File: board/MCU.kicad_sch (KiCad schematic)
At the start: 19 parts, among them J1 DEBUG, Q1 NMOS, Q2 BSS138, U4 LT1910, U7 ESP32-S2-DEVKITM-1U

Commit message: Add TFT Molex Connector
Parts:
- C3: footprint (none) -> Capacitor_SMD:C_0603_1608Metric_Pad1.08x0.95mm_HandSolder
- R16, R17, R3: footprint (none) -> Resistor_SMD:R_0603_1608Metric_Pad0.98x0.95mm_HandSolder
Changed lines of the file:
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@@
 			)
 		)
-		(property "Footprint" ""
+		(property "Footprint" "Capacitor_SMD:C_0603_1608Metric_Pad1.08x0.95mm_HandSolder"
 			(at 144.78 166.37 0)
 			(effects
@@
 			)
 		)
-		(property "Footprint" ""
+		(property "Footprint" "Resistor_SMD:R_0603_1608Metric_Pad0.98x0.95mm_HandSolder"
 			(at 241.046 34.544 90)
 			(effects
@@
 			)
 		)
-		(property "Footprint" ""
+		(property "Footprint" "Resistor_SMD:R_0603_1608Metric_Pad0.98x0.95mm_HandSolder"
 			(at 246.634 34.036 90)
 			(effects
@@
 			)
 		)
-		(property "Footprint" ""
+		(property "Footprint" "Resistor_SMD:R_0603_1608Metric_Pad0.98x0.95mm_HandSolder"
 			(at 108.966 143.764 90)
 			(effects

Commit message: Add Footprint Assignments
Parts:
- B1: footprint (none) -> MRDT_Devices:BUZZER_SMI_1324_TW_5V_2_R
- C5: footprint Capacitor_SMD:C_0603_1608Metric_Pad1.08x0.95mm_HandSolder -> Capacitor_THT:CP_Radial_D10.0mm_P5.00mm
- Conn5: footprint MRDT_Connectors:MOLEX_SL_04_Vertical -> MRDT_Connectors:MOLEX_SL_09_Horizontal
- Conn6: footprint (none) -> MRDT_Connectors:MOLEX_SL_07_Horizontal
- J1: footprint (none) -> Connector_PinSocket_2.54mm:PinSocket_1x04_P2.54mm_Vertical
- Molex4_1, Molex4_4, Molex4_6, Molex4_7: footprint MRDT_Connectors:MOLEX_SL_04_Vertical -> MRDT_Connectors:MOLEX_SL_04_Horizontal
- Q1: footprint (none) -> Package_TO_SOT_THT:TO-220-3_Vertical
- U4: footprint (none) -> Package_SO:SOIC-8_3.9x4.9mm_P1.27mm
- U7: footprint ESP32-S2-DEVKITM-1U:XCVR_ESP32-S2-DEVKITM-1U -> MRDT_Shields:XCVR_ESP32-S2-DEVKITM-1U
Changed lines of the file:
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@@
 			)
 		)
-		(property "Footprint" ""
+		(property "Footprint" "MRDT_Devices:BUZZER_SMI_1324_TW_5V_2_R"
 			(at 46.99 167.64 0)
 			(effects
@@
 			)
 		)
-		(property "Footprint" ""
+		(property "Footprint" "MRDT_Connectors:MOLEX_SL_07_Horizontal"
 			(at 218.44 119.38 0)
 			(effects
@@
 			)
 		)
-		(property "Footprint" "MRDT_Connectors:MOLEX_SL_04_Vertical"
+		(property "Footprint" "MRDT_Connectors:MOLEX_SL_04_Horizontal"
 			(at 257.81 46.99 0)
 			(effects
@@
 			)
 		)
-		(property "Footprint" "Capacitor_SMD:C_0603_1608Metric_Pad1.08x0.95mm_HandSolder"
+		(property "Footprint" "Capacitor_THT:CP_Radial_D10.0mm_P5.00mm"
 			(at 44.1452 93.98 0)
 			(effects
@@
 			)
 		)
-		(property "Footprint" "MRDT_Connectors:MOLEX_SL_04_Vertical"
+		(property "Footprint" "MRDT_Connectors:MOLEX_SL_04_Horizontal"
 			(at 266.7 74.93 0)
 			(effects
@@
 			)
 		)
-		(property "Footprint" "MRDT_Connectors:MOLEX_SL_04_Vertical"
+		(property "Footprint" "MRDT_Connectors:MOLEX_SL_04_Horizontal"
 			(at 264.16 138.43 0)
 			(effects
@@
 			)
 		)
-		(property "Footprint" ""
+		(property "Footprint" "Package_TO_SOT_THT:TO-220-3_Vertical"
 			(at 165.1 157.48 0)
 			(effects
@@
 			)
 		)
-		(property "Footprint" "MRDT_Connectors:MOLEX_SL_04_Vertical"
+		(property "Footprint" "MRDT_Connectors:MOLEX_SL_09_Horizontal"
 			(at 22.86 50.8 0)
 			(effects
@@
 			)
 		)
-		(property "Footprint" "MRDT_Connectors:MOLEX_SL_04_Vertical"
+		(property "Footprint" "MRDT_Connectors:MOLEX_SL_04_Horizontal"
 			(at 266.7 109.22 0)
 			(effects
@@
 			)
 		)
-		(property "Footprint" ""
+		(property "Footprint" "Package_SO:SOIC-8_3.9x4.9mm_P1.27mm"
 			(at 118.11 162.56 0)
 			(effects
@@
 			)
 		)
-		(property "Footprint" ""
+		(property "Footprint" "Connector_PinSocket_2.54mm:PinSocket_1x04_P2.54mm_Vertical"
 			(at 213.36 34.29 0)
 			(effects
@@
 			)
 		)
-		(property "Footprint" "ESP32-S2-DEVKITM-1U:XCVR_ESP32-S2-DEVKITM-1U"
+		(property "Footprint" "MRDT_Shields:XCVR_ESP32-S2-DEVKITM-1U"
 			(at 127 64.77 0)
 			(effects

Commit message: Add Layout
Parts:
- Conn2, Conn3: footprint MRDT_Connectors:Anderson_2_Horizontal_Side_by_Side -> MRDT_Connectors:Square_Anderson_2_H_Side_By_Side_PV
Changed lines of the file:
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@@
 			)
 		)
-		(property "Footprint" "MRDT_Connectors:Anderson_2_Horizontal_Side_by_Side"
+		(property "Footprint" "MRDT_Connectors:Square_Anderson_2_H_Side_By_Side_PV"
 			(at 30.48 139.7 0)
 			(effects
@@
 			)
 		)
-		(property "Footprint" "MRDT_Connectors:Anderson_2_Horizontal_Side_by_Side"
+		(property "Footprint" "MRDT_Connectors:Square_Anderson_2_H_Side_By_Side_PV"
 			(at 22.86 113.03 0)
 			(effects
@@
 			)
 		)
-		(property "Footprint" "MRDT_Connectors:Anderson_2_Horizontal_Side_by_Side"
+		(property "Footprint" "MRDT_Connectors:Square_Anderson_2_H_Side_By_Side_PV"
 			(at 22.86 101.6 0)
 			(effects
@@
 			)
 		)
-		(property "Footprint" "MRDT_Connectors:Anderson_2_Horizontal_Side_by_Side"
+		(property "Footprint" "MRDT_Connectors:Square_Anderson_2_H_Side_By_Side_PV"
 			(at 30.48 148.59 0)
 			(effects

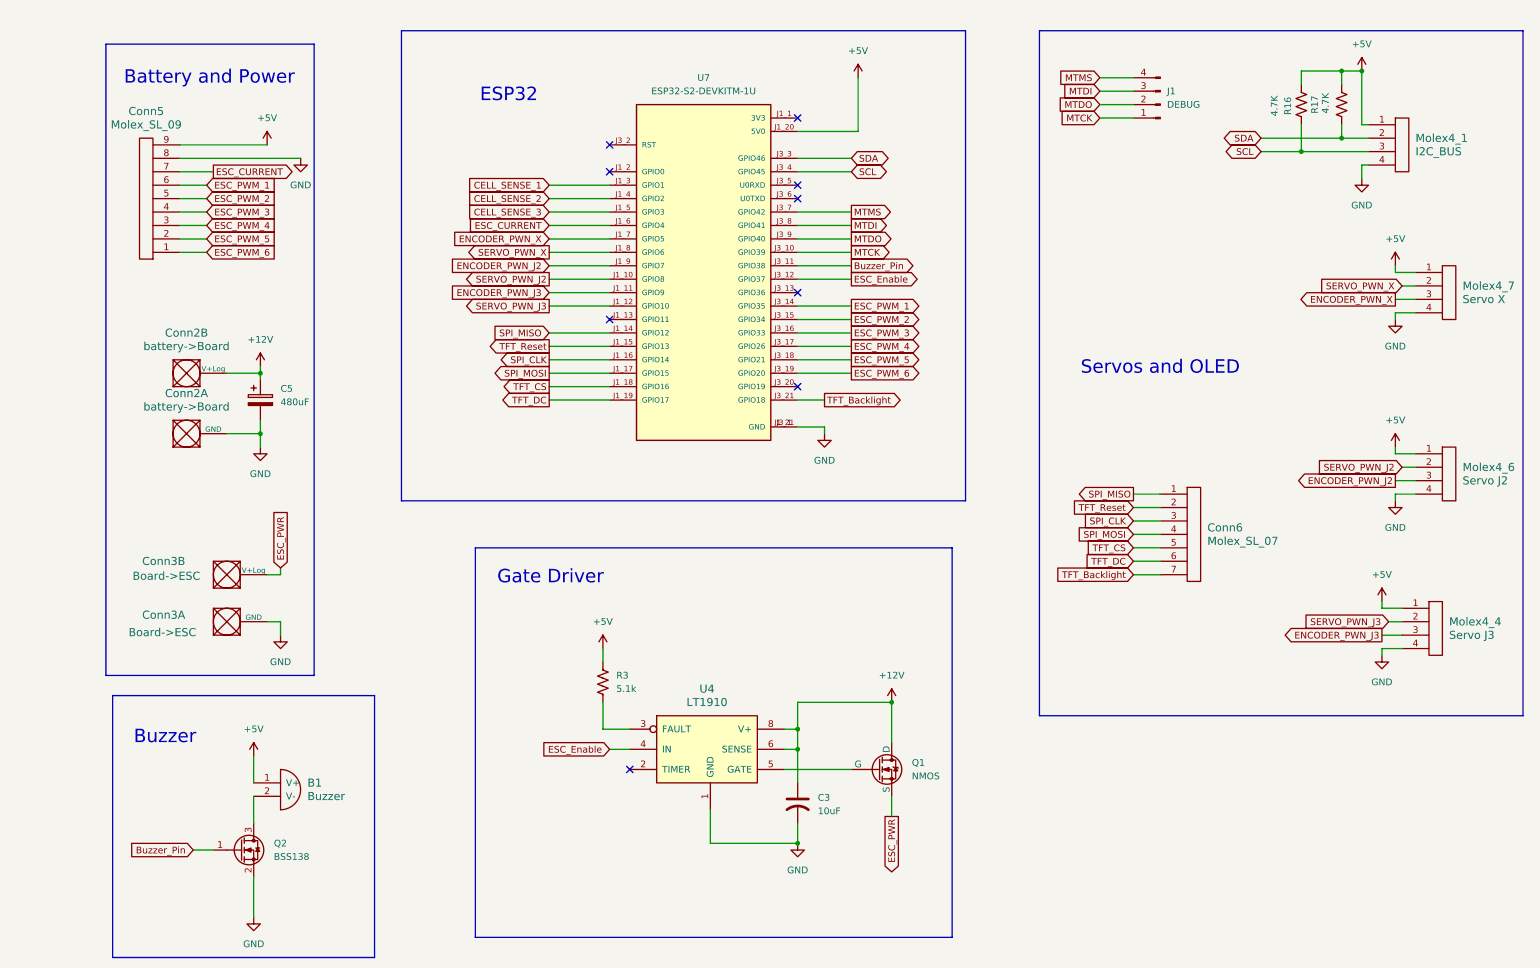
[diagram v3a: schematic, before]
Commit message: added pmos channel (still need footprints not working)
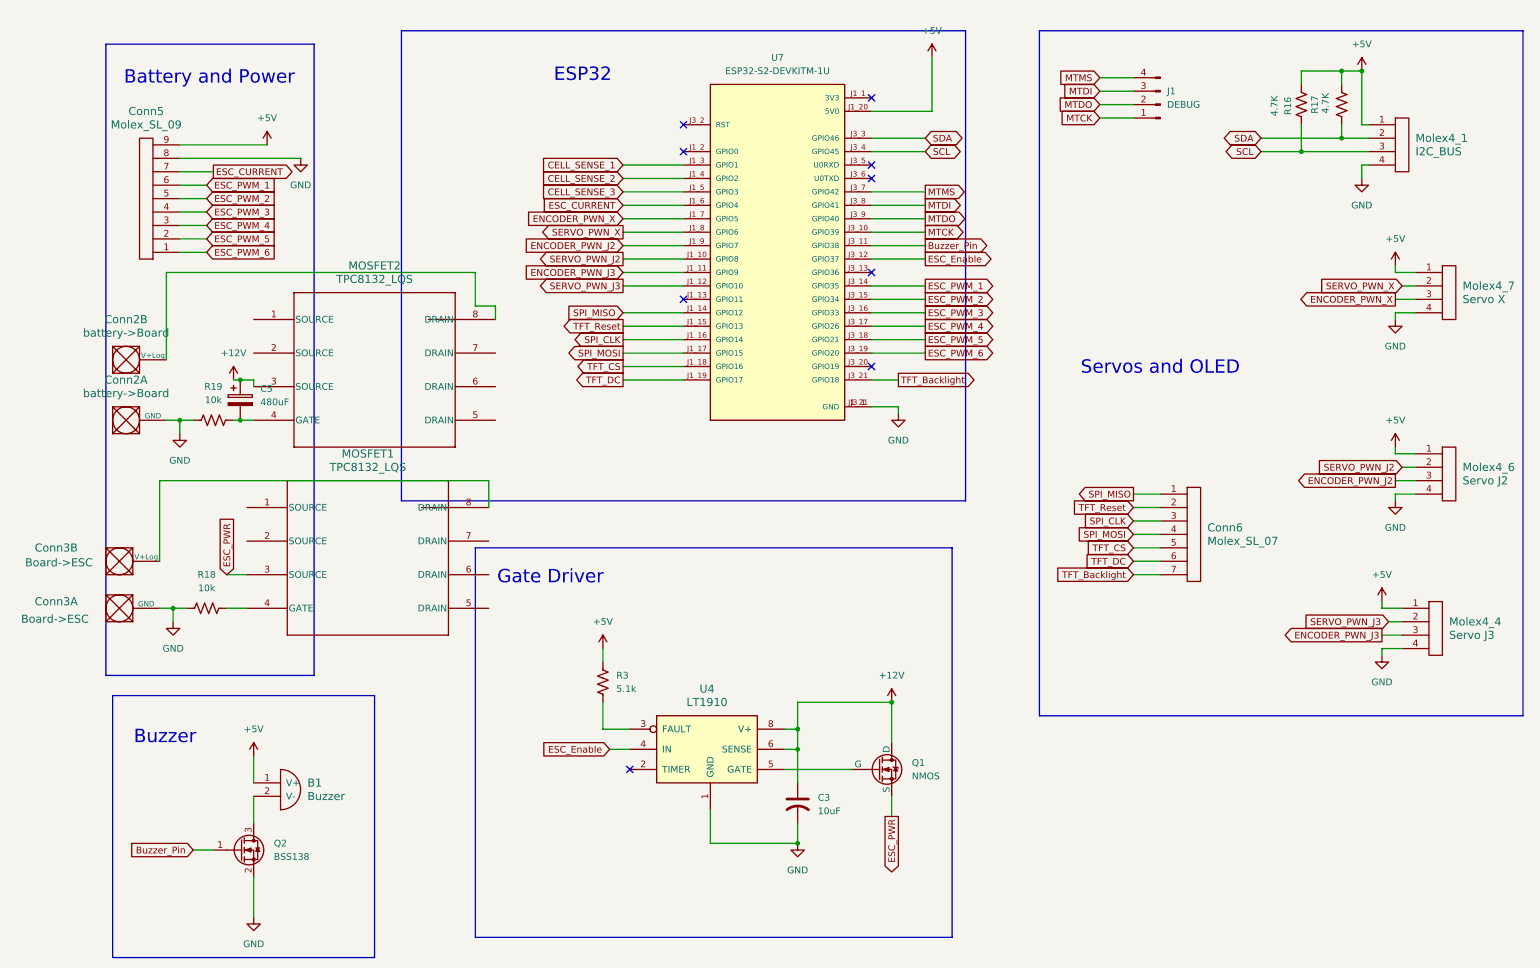
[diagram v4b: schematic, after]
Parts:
- added MOSFET1, MOSFET2: TPC8132_LQS, MRDT_Devices:SOP-8_TOS-L, symbol MRDT_Devices:TPC8132_LQS
- added R18, R19: 10k, symbol Device:R_US
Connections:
- net +12V: now also MOSFET2.3 (SOURCE); no longer Conn2.2 (V+Log)
- net ESC_PWR: now also MOSFET1.3 (SOURCE); no longer Conn3.2 (V+Log)
- net GND: now also R18.1, R19.1; no longer C5.2
- new net: Conn3.2 (V+Log), MOSFET1.8 (DRAIN)
- new net: C5.2, MOSFET2.4 (GATE), R19.2
- new net: MOSFET1.4 (GATE), R18.2
- new net: Conn2.2 (V+Log), MOSFET2.8 (DRAIN)
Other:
- moved on the sheet: C5, Conn2A, Conn2B, Conn3A, Conn3B, U7

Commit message: Add resistor footprints for p-channel mosfets
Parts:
- MOSFET2: footprint MRDT_Devices:SOP-8_TOS-L -> MRDT_Devices:TPC8132_LQ_S
- R18, R19: footprint (none) -> Resistor_SMD:R_0603_1608Metric_Pad0.98x0.95mm_HandSolder
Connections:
- no-connect marks 9 -> 19
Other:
- moved on the sheet: C3, C5, Conn2A, Conn2B, Conn3A, Conn3B, Conn6, MOSFET1, MOSFET2, Molex4_4, Molex4_6, Q1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

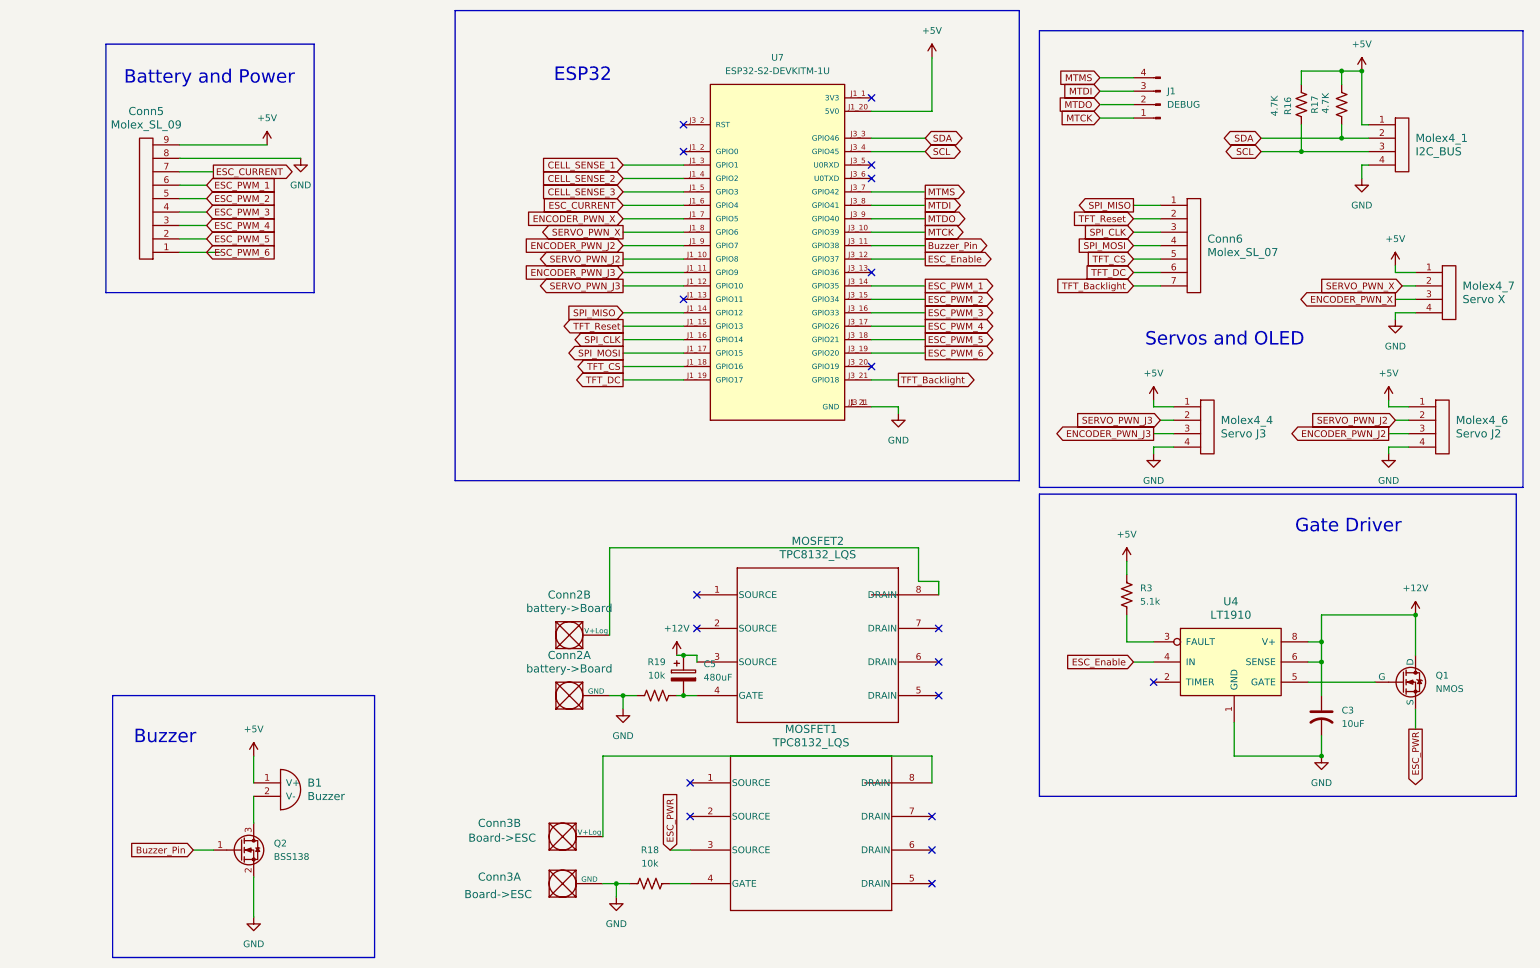
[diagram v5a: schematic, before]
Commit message: Add p-channel MOSFETs to Layout
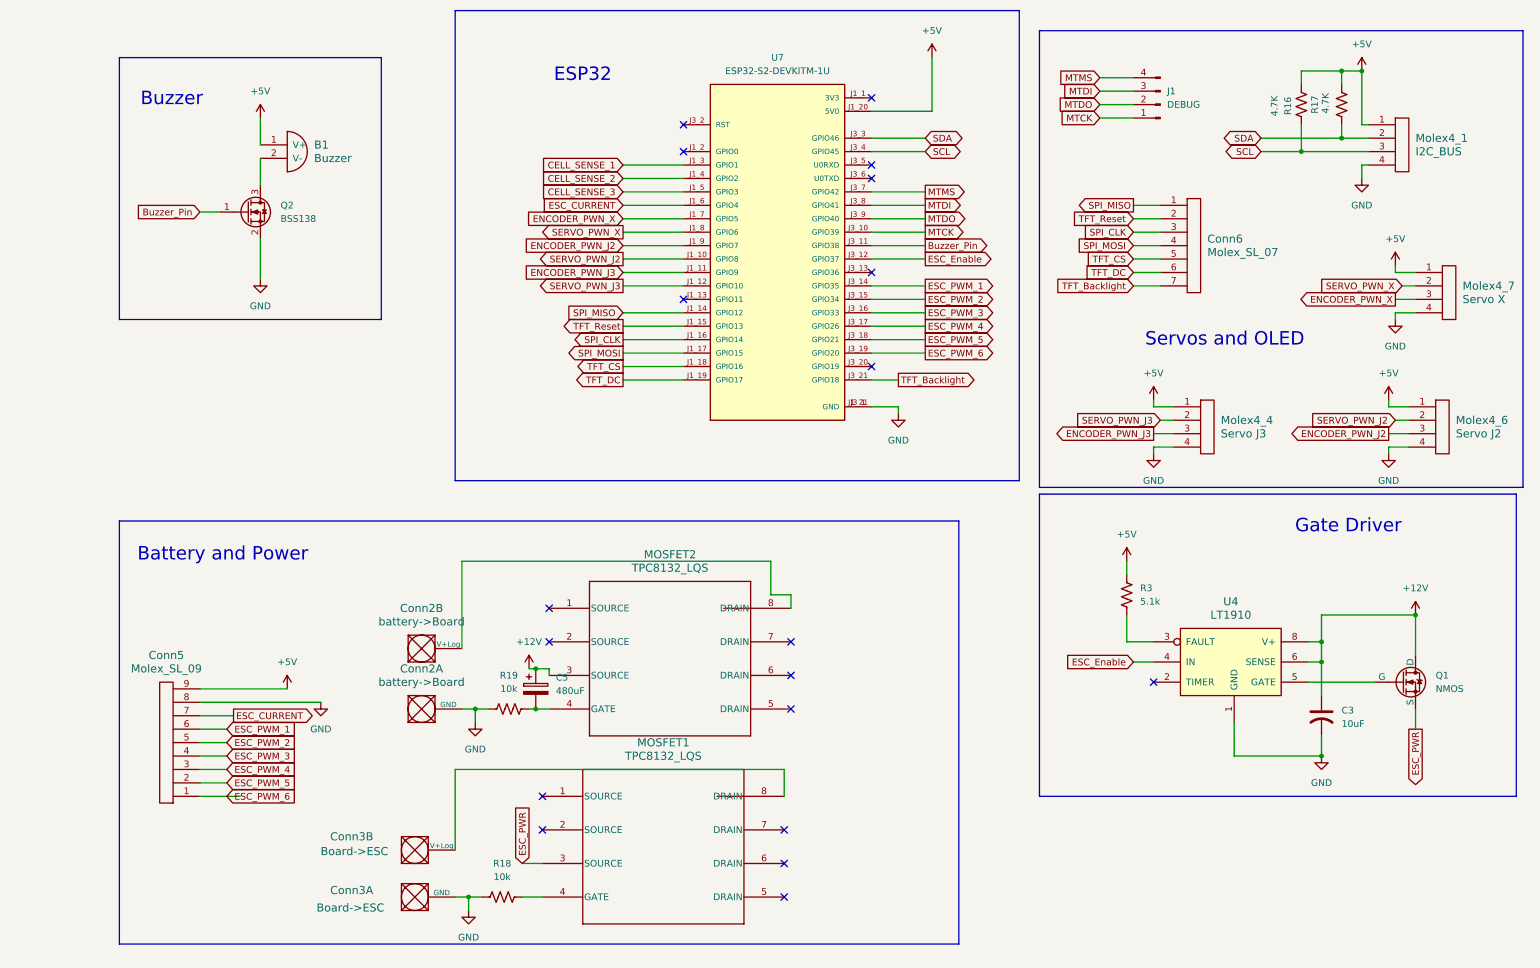
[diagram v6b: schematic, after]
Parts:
- MOSFET2: footprint MRDT_Devices:TPC8132_LQ_S -> MRDT_Devices:SOP-8_TOS-L
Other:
- moved on the sheet: B1, C5, Conn2A, Conn2B, Conn3A, Conn3B, Conn5, MOSFET1, Q2, R18, R19

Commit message: Layout started with initial dimensions
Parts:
- added H1, H2, H3, H4: MountingHole, MRDT_Drill_Holes:4_40_Hole, symbol Mechanical:MountingHole
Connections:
- net +12V: now also MOSFET2.1 (SOURCE), MOSFET2.2 (SOURCE)
- net ESC_PWR: now also MOSFET1.1 (SOURCE), MOSFET1.2 (SOURCE)
- net at MOSFET2.5 (DRAIN): now also Conn2.2 (V+Log), MOSFET2.6 (DRAIN), MOSFET2.7 (DRAIN), MOSFET2.8 (DRAIN)
- net at Conn3.2 (V+Log), MOSFET1.8 (DRAIN): now also MOSFET1.5 (DRAIN), MOSFET1.6 (DRAIN), MOSFET1.7 (DRAIN)
- no-connect marks 19 -> 9
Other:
- moved on the sheet: C5

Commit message: Move OpAmps and Changed buzzer footprint
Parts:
- B1: footprint MRDT_Devices:BUZZER_SMI_1324_TW_5V_2_R -> Buzzer_Beeper:Buzzer_12x9.5RM7.6
